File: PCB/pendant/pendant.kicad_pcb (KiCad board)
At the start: 2 copper layers, 45.5 x 54 mm, 13 parts, among them J1 Conn_02x10_Odd_Even, J2 Conn_01x12, J3 Conn_01x03, J4 Conn_01x02, Q1 2N3904, Q2 2N3904, U1 Pico

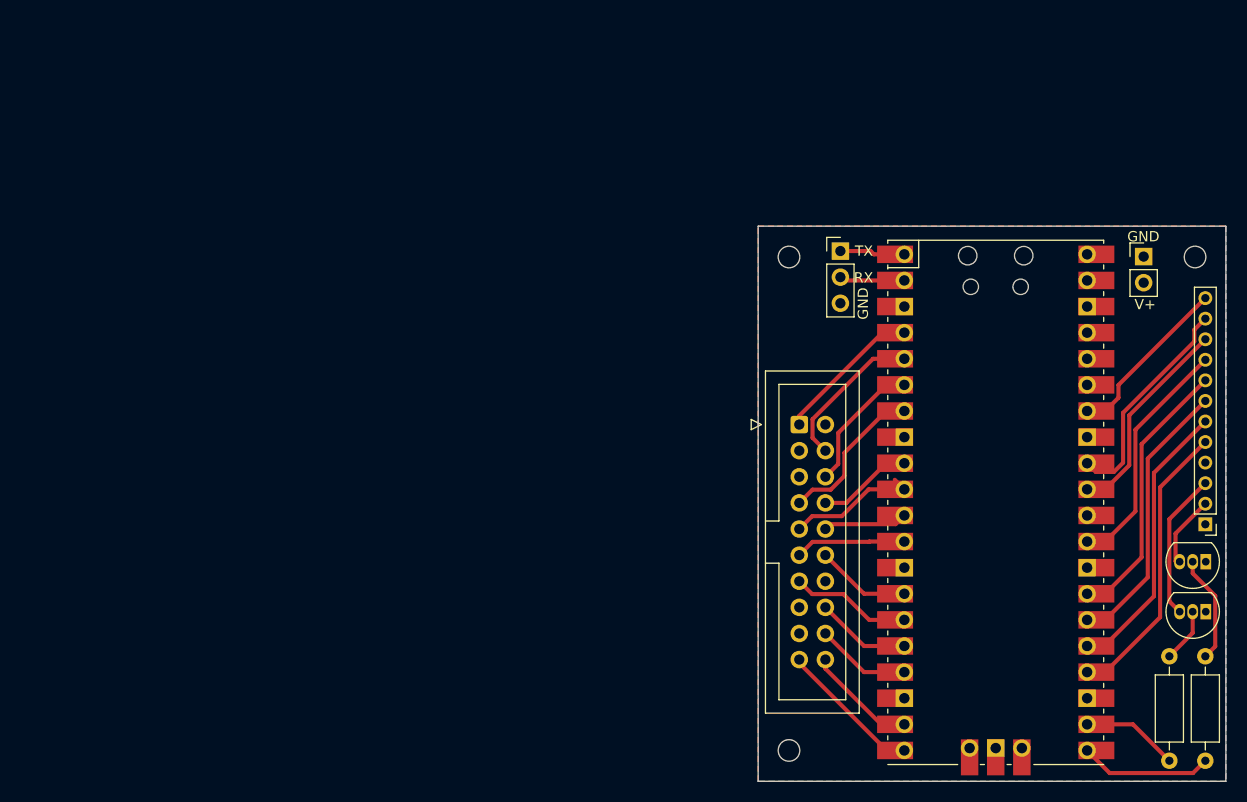
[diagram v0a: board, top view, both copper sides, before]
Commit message: feat: Redesign Pendant circuit and add stepper control circuit
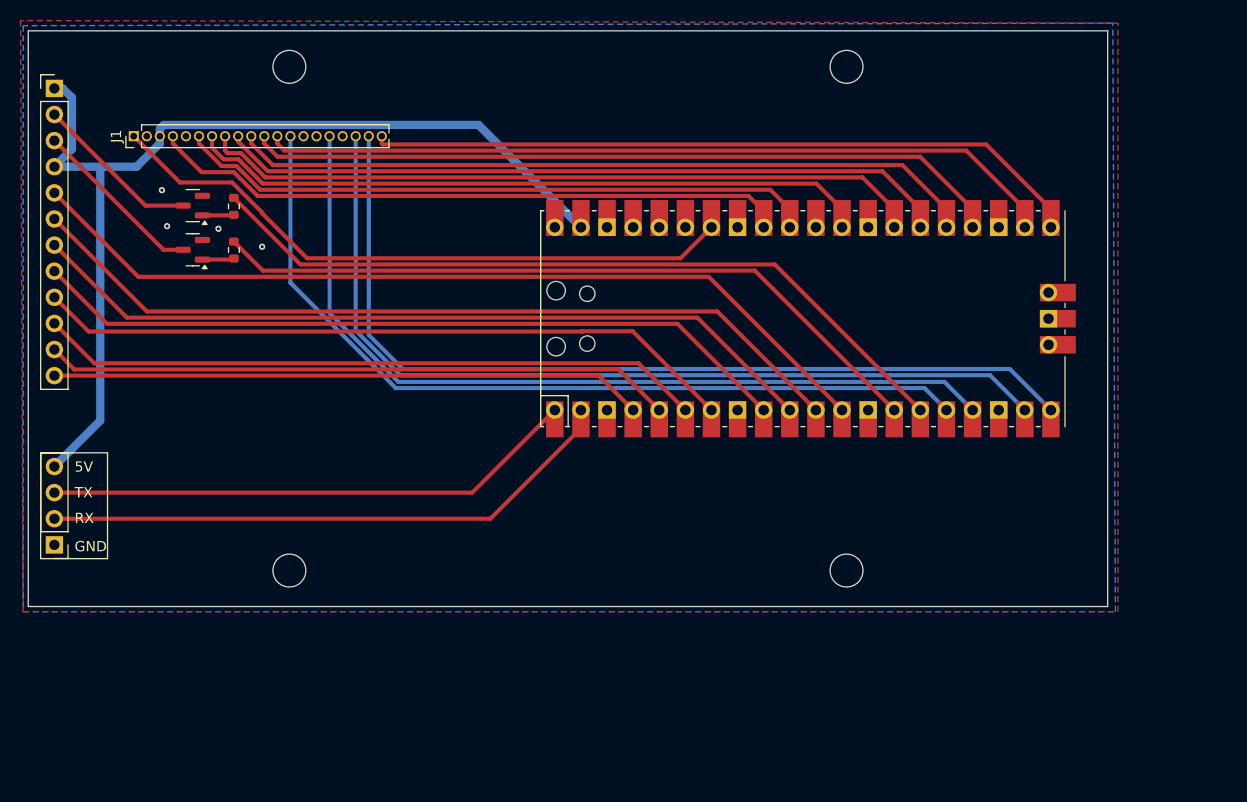
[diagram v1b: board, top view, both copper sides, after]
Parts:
- removed G***: LOGO, LOGO
- removed J3: Conn_01x03, Connector_PinHeader_2.54mm:PinHeader_1x03_P2.54mm_Vertical
- removed J4: Conn_01x02, Connector_PinHeader_2.54mm:PinHeader_1x02_P2.54mm_Vertical
- removed the REF** at (124.0, 120.0)
- removed the REF** at (124.0, 72.0)
- removed the REF** at (163.5, 72.0)
- added J5: Conn_01x04, Connector_PinHeader_2.54mm:PinHeader_1x04_P2.54mm_Vertical, F.Cu at (52.5, 100.0)
- added REF**: MountingHole_3.2mm_M3, MountingHole:MountingHole_3.2mm_M3, F.Cu at (75.4, 53.5)
- added REF**: MountingHole_3.2mm_M3, MountingHole:MountingHole_3.2mm_M3, F.Cu at (75.4, 102.5)
- added REF**: MountingHole_3.2mm_M3, MountingHole:MountingHole_3.2mm_M3, F.Cu at (129.6, 102.5)
- added REF**: MountingHole_3.2mm_M3, MountingHole:MountingHole_3.2mm_M3, F.Cu at (129.6, 53.5)
- J1: footprint Connector_IDC:IDC-Header_2x10_P2.54mm_Vertical -> Connector_PinHeader_1.27mm:PinHeader_1x20_P1.27mm_Vertical
- J2: footprint Connector_PinHeader_2.00mm:PinHeader_1x12_P2.00mm_Vertical -> Connector_PinHeader_2.54mm:PinHeader_1x12_P2.54mm_Vertical
- Q1, Q2: value 2N3904 -> MMBT3904-7-F; footprint Package_TO_SOT_THT:TO-92_Inline -> Package_TO_SOT_SMD:SOT-23
- R1, R2: footprint Resistor_THT:R_Axial_DIN0207_L6.3mm_D2.5mm_P10.16mm_Horizontal -> Resistor_SMD:R_0603_1608Metric
- moved J2 119.7 mm to (52.5, 55.6), turned to 0 degrees
- moved R1 108.8 mm to (70.0, 67.1), turned to -90 degrees
- moved Q2 104.6 mm to (66.0, 71.3)
- moved Q1 104.5 mm to (66.0, 67.0)
- moved R2 103.7 mm to (70.0, 71.3), turned to -90 degrees
- moved J1 70.6 mm to (60.3, 60.2), turned to 90 degrees
- moved U1 25.9 mm to (125.3, 78.0), turned to 90 degrees
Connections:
- Q1 pad 1: GND -> Net-(Q1-B)
- Q1 pad 2: Net-(Q1-B) -> GND
- Q2 pad 1: GND -> Net-(Q2-B)
- Q2 pad 2: Net-(Q2-B) -> GND
- U1 pad 10: Digit 9 -> COL 2
- U1 pad 11: D -> COL 1
- U1 pad 12: Digit 8 -> PEN BTN
- U1 pad 14: A -> PEN LED CTRL
- U1 pad 15: Digit 7 -> PWR LED CTRL
- U1 pad 16: Digit 2 -> Digit 7
- U1 pad 17: Digit 4 -> Digit 2
- U1 pad 19: Digit 3 -> Digit 4
- U1 pad 21: PWR LED CTRL -> Digit 3
- U1 pad 22: PEN LED CTRL -> A
- U1 pad 24: PEN BTN -> Digit 8
- U1 pad 25: COL 1 -> D
- U1 pad 26: COL 2 -> Digit 9
- U1 pad 27: COL 3 -> C
- U1 pad 29: COL 4 -> Digit 10
- U1 pad 31: COL 5 -> B
- U1 pad 32: ROW 1 -> RESET BTN
- U1 pad 34: ROW 2 -> PAPER HOLD BTN
- U1 pad 4: PAPER HOLD BTN -> ROW 2
- U1 pad 5: RESET BTN -> ROW 1
- U1 pad 6: B -> COL 5
- U1 pad 7: Digit 10 -> COL 4
- U1 pad 9: C -> COL 3
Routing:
- net +5V: track 0.00 -> 98.4 mm
- net Digit 4: track 9.24 -> 87.2 mm
- net Digit 2: track 9.24 -> 83.7 mm
- net Digit 5: track 16.0 -> 88.7 mm
- net Digit 7: track 11.8 -> 83.2 mm
- net A: track 9.24 -> 77.8 mm
- net D: track 8.23 -> 72.7 mm
- net Digit 8: track 10.8 -> 74.0 mm
- net PWR LED CTRL: track 12.9 -> 75.3 mm
- net PEN LED CTRL: track 9.47 -> 71.0 mm
- net C: track 9.73 -> 70.6 mm
- net Digit 3: track 10.8 -> 70.2 mm
- net Digit 9: track 13.1 -> 71.4 mm
- net PEN BTN: track 28.2 -> 85.4 mm
- net COL 1: track 27.6 -> 81.8 mm
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- added copper zone on F.Cu, net GND
- removed copper zone on F.Cu, net +5V
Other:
- board size 45.5 x 54 mm -> 105 x 56 mm
- board text added: "5V"
- board text removed: "V+"
